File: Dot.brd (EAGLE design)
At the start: 25.4 x 31.5 mm, 43 parts, among them IC1 CAT24M010TS, IC2 SI1145, U1 ATMEGA328P-MU-QFN32, U2 TMP102, U3 ISL29125, U4 9DoF IMU, U5 BMP18

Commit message: Add C10 1000uF with enough room, move HexID to other side
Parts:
- removed SJ1: SOLDERJUMPERNO, SparkFun:SJ_2S-NO
- added C10: 1500uF 4V, adafruit:CT7343
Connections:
- removed net N$2: IC1.A1, SJ1.1
- net +3V3: now also C10.+; no longer SJ1.2
- net GND: now also C10.-
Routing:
- net +3V3: track 132.8 -> 139.8 mm
- net N$2: track 2.90 -> 0.00 mm, vias 1 -> 0
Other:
- board text removed: "EEP"

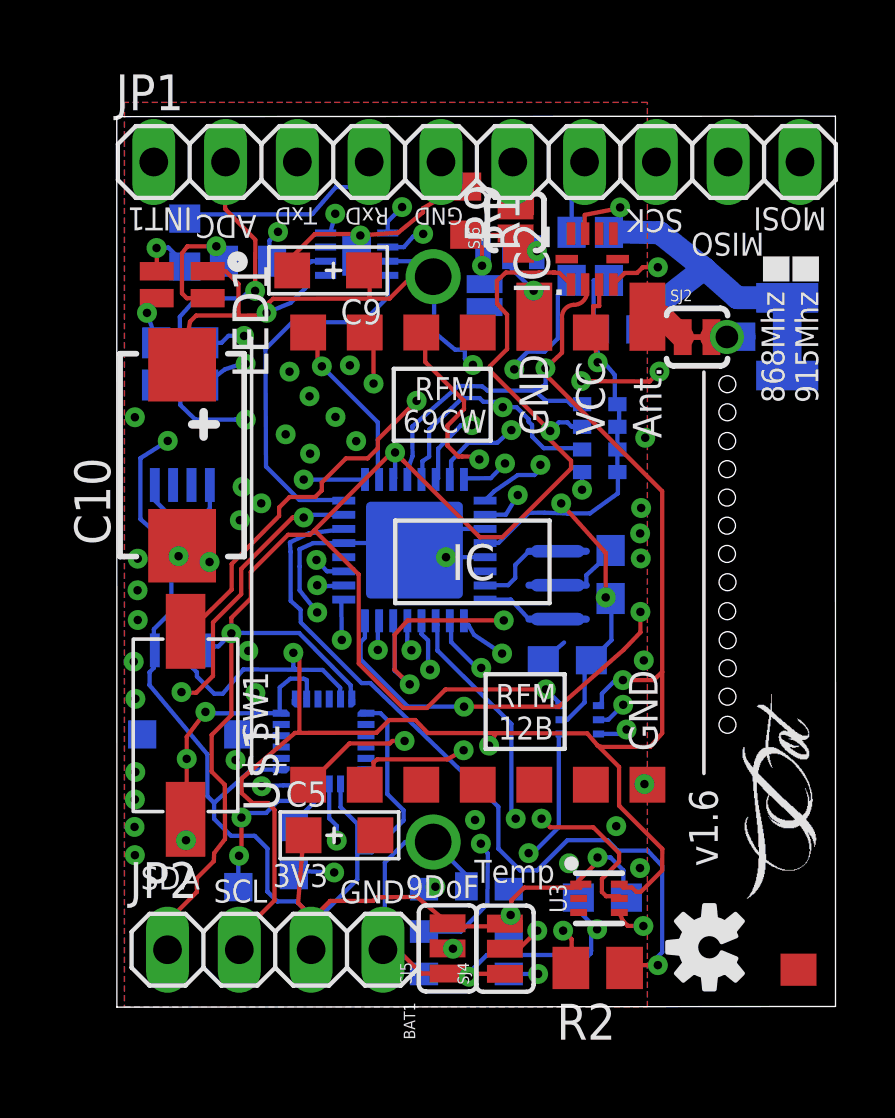
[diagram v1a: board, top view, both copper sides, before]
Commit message: Remove C9 100uF add Zenner 3.6V
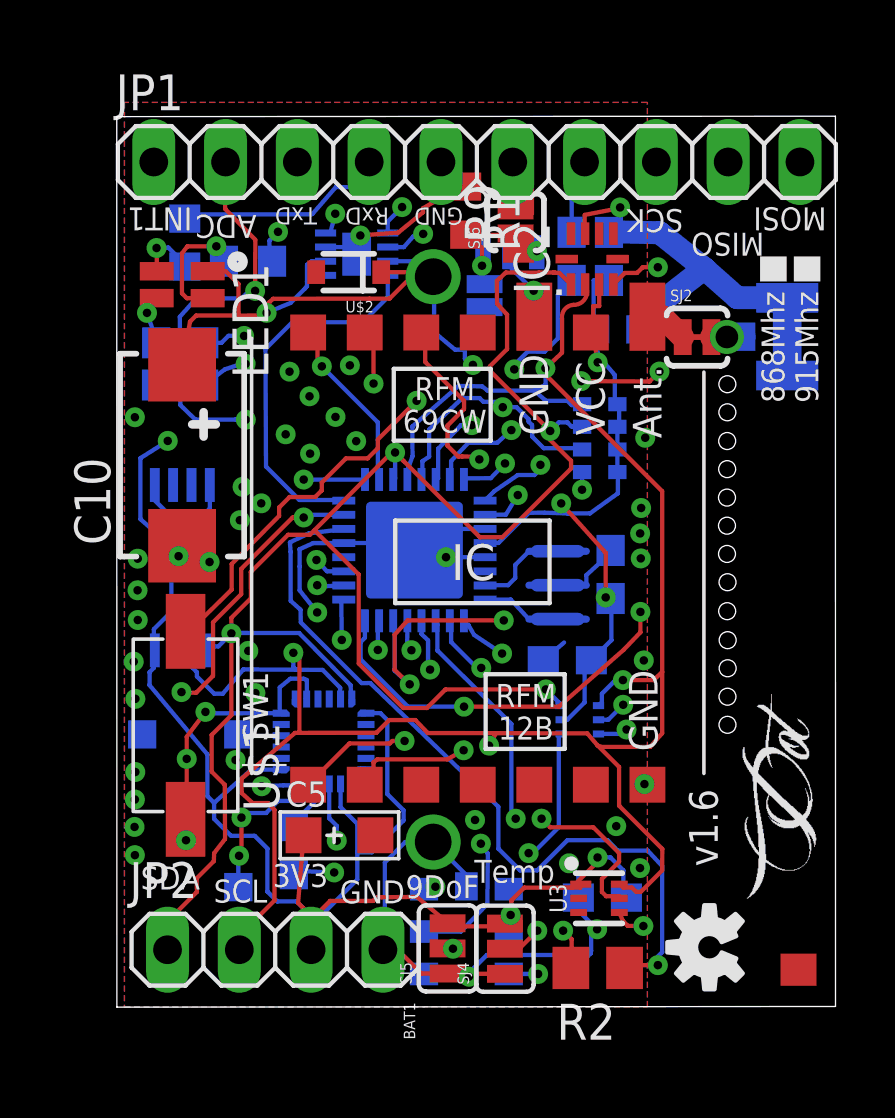
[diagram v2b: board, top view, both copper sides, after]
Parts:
- removed C9: 100uf, Seeed-OPL-Capacitor:AVX-A
- added U$2: DIODE-ZENER-BZT52, SparkFun:SOD-323
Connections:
- net +3V3: now also U$2.1; no longer C9.+
- net GND: now also U$2.2; no longer C9.-
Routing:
- net GND: track 129.3 -> 126.1 mm
- net +3V3: track 139.8 -> 140.5 mm
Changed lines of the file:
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@@
 <text x="23.9776" y="21.8948" size="0.8128" layer="21" rot="R90">868Mhz</text>
 <text x="25.1714" y="21.8948" size="0.8128" layer="21" rot="R90">915Mhz</text>
-<rectangle x1="24.257" y1="26.1874" x2="25.1968" y2="27.0764" layer="21"/>
-<rectangle x1="23.2156" y1="26.1874" x2="24.1554" y2="27.0764" layer="21"/>
+<rectangle x1="24.3078" y1="26.1874" x2="25.2476" y2="27.0764" layer="21"/>
+<rectangle x1="23.114" y1="26.1874" x2="24.0538" y2="27.0764" layer="21"/>
 <rectangle x1="22.479" y1="26.6192" x2="25.5016" y2="28.5242" layer="22"/>
 <text x="22.1234" y="28.6766" size="0.6096" layer="22" rot="SMR270">HexID</text>
@@
 <element name="U$4" library="LDCL015" package="SOT23-5" value="LDCL015" x="14.263115625" y="25.92196875" rot="MR180"/>
 <element name="LED1" library="led" package="GM1WA55311A" value="GM1WA55311A" x="2.670809375" y="26.074628125" rot="R270"/>
-<element name="C9" library="Seeed-OPL-Capacitor" package="AVX-A" value="100uf" x="7.832090625" y="26.579578125" rot="R180">
-<attribute name="MPN" value="TLJA107M006R0800" x="7.832090625" y="26.579578125" size="1.778" layer="27" rot="R180" display="off"/>
-</element>
 <element name="SJ2" library="SparkFun" package="SJ_2S-TRACE" value="SOLDERJUMPERTRACE" x="20.884871875" y="24.221084375"/>
 <element name="C5" library="Seeed-OPL-Capacitor" package="AVX-A" value="100uf" x="8.2339125" y="6.5955625">
@@
 <element name="Y1" library="SparkFun-Clocks" package="RESONATOR-SMD-3.2X1.3" value="" x="15.9512" y="15.4432" rot="MR90"/>
 <element name="C10" library="adafruit" package="CT7343" value="1500uF 4V" x="2.667" y="20.0406" rot="R90"/>
+<element name="U$2" library="SparkFun" package="SOD-323" value="DIODE-ZENER-BZT52" x="8.5598" y="26.5176" rot="R180"/>
 </elements>
 <signals>
@@
 <wire x1="7.416546875" y1="5.284671875" x2="6.830009375" y2="5.871209375" width="0.1524" layer="2"/>
 <wire x1="6.830009375" y1="5.871209375" x2="4.6822375" y2="5.871209375" width="0.1524" layer="2"/>
-<contactref element="C9" pad="-"/>
-<wire x1="6.562090625" y1="26.579578125" x2="6.562090625" y2="27.06481875" width="0.1524" layer="1"/>
-<wire x1="6.562090625" y1="27.06481875" x2="7.36325625" y2="27.865984375" width="0.1524" layer="1"/>
-<wire x1="7.36325625" y1="27.865984375" x2="8.975440625" y2="27.86745625" width="0.1524" layer="1"/>
 <wire x1="8.975440625" y1="27.86745625" x2="8.971378125" y2="27.81638125" width="0.1524" layer="1"/>
 <contactref element="C5" pad="-"/>
@@
 <contactref element="C10" pad="-"/>
 <via x="0.996696875" y="21.38553125" extent="1-16" drill="0.3"/>
+<contactref element="U$2" pad="2"/>
 <wire x1="16.1884375" y1="13.40993125" x2="16.182075" y2="13.41629375" width="0" layer="19" extent="15-16"/>
 </signal>
@@
 <wire x1="5.6873125" y1="6.125209375" x2="5.6873125" y2="4.618228125" width="0.1524" layer="16"/>
 <wire x1="5.6873125" y1="4.618228125" x2="5.68045625" y2="4.611371875" width="0.1524" layer="16"/>
-<contactref element="C9" pad="+"/>
-<wire x1="9.102090625" y1="26.579578125" x2="9.302553125" y2="26.579578125" width="0.1524" layer="1"/>
-<wire x1="9.302553125" y1="26.579578125" x2="9.302553125" y2="25.580578125" width="0.1524" layer="1"/>
 <wire x1="4.66681875" y1="24.98031875" x2="4.6663625" y2="24.98283125" width="0.1524" layer="1"/>
 <wire x1="4.6663625" y1="24.98283125" x2="4.66133125" y2="26.101496875" width="0.1524" layer="1"/>
@@
 <wire x1="2.159" y1="20.5486" x2="3.5138375" y2="20.5486" width="0.1524" layer="15"/>
 <wire x1="3.5138375" y1="20.5486" x2="3.5646375" y2="20.4978" width="0.1524" layer="15"/>
+<contactref element="U$2" pad="1"/>
+<wire x1="9.7098" y1="26.5176" x2="11.389646875" y2="26.5176" width="0.1524" layer="1"/>
+<wire x1="11.389646875" y1="26.5176" x2="11.54885625" y2="26.358390625" width="0.1524" layer="1"/>
 <wire x1="13.38685625" y1="16.934390625" x2="13.38685625" y2="15.934390625" width="0" layer="19" extent="16-16"/>
 </signal>
